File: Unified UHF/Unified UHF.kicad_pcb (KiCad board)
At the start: 2 copper layers, 82.5 x 82.5 mm, 82 parts, among them IC1 QPC1022SR, IC2 GRF5504, IC3 LHA-13LN+, IC4 QPC1022SR, J1 Conn_01x05, J2 Conn_01x02, J3 Conn_01x02, J4 Conn_01x01, J5 PCB.SMAFST.2H.A.HT, U1 AT86RF215-ZU, U2 NCS-62+, X1 TYETACSANF-26.000000

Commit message: small changes
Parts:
- H1, H2, H3, H4: footprint MountingHole:MountingHole_3.2mm_M3 -> MountingHole:MountingHole_3.5mm_Pad
- moved C4 0.58 mm to (37.8, 66.1)
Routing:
- net GND: track 198.8 -> 189.3 mm, vias 2973 -> 2977

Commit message: Routed coax
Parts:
- moved J5 5.60 mm to (88.0, 26.2)
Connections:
- C3 pad 1: GND -> GNDD
- C4 pad 1: GND -> GNDD
- C5 pad 1: GND -> GNDD
- C6 pad 1: GND -> GNDD
- U1 pad 20: GND -> GNDD
- U1 pad 23: GND -> GNDD
- U1 pad 24: GND -> GNDD
- U1 pad 32: GND -> GNDD
- U1 pad 38: GND -> GNDD
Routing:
- net Net-(IC4-ANT): track 4.63 -> 46.9 mm
- net GND: track 189.3 -> 162.8 mm, vias 2977 -> 3321
- net GNDD: track 0.00 -> 14.5 mm, vias 0 -> 8
- net Net-(U1-RFN09): track 8.53 -> 7.21 mm
- net Net-(U1-FEA09): track 36.3 -> 37.4 mm, vias 1 -> 0
- added copper zone on B.Cu, net GNDD
- added copper zone on F.Cu, net GNDD
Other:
- board text added: "PVDX UHF BOARD"
- board text removed: "PVDX UHF FRONTEND"

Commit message: adjustments
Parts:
- moved J5 67.6 mm to (88.2, 93.8)
- moved G*** 33.9 mm to (55.0, 87.2)
- moved C28 7.83 mm to (100.8, 68.4)
- moved TP13 7.41 mm to (101.8, 61.0)
- moved C25 7.36 mm to (101.6, 71.2), turned to 0 degrees
- moved C24 4.45 mm to (101.6, 73.2), turned to 0 degrees
- moved TP14 2.89 mm to (104.6, 53.4)
- moved L5 1.77 mm to (100.4, 75.2)
- moved C3 1.52 mm to (39.4, 53.8), turned to 0 degrees
- moved L4 1.50 mm to (97.6, 74.2)
- moved TP2 1.34 mm to (35.6, 55.2)
- moved C5 1.14 mm to (35.4, 60.6), turned to 90 degrees
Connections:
- H1 pad 1: (no net) -> GND
- H2 pad 1: (no net) -> GND
- H3 pad 1: (no net) -> GND
- H4 pad 1: (no net) -> GND
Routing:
- net Net-(IC4-RF1): track 27.2 -> 19.7 mm
- net Net-(IC4-ANT): track 46.9 -> 53.5 mm
- net Net-(C24-Pad1): track 7.76 -> 4.06 mm
- net +5V: track 143.1 -> 141.6 mm
- net +3V3: track 112.0 -> 113.2 mm
- net Net-(IC2-RF_OUT/VCC2_1): track 7.26 -> 6.18 mm
- net Net-(U1-CLKO): track 5.56 -> 6.41 mm
- net GND: track 162.8 -> 162.6 mm, vias 3321 -> 2852
- removed copper zone on B.Cu, net GNDD
- removed copper zone on F.Cu, net GNDD

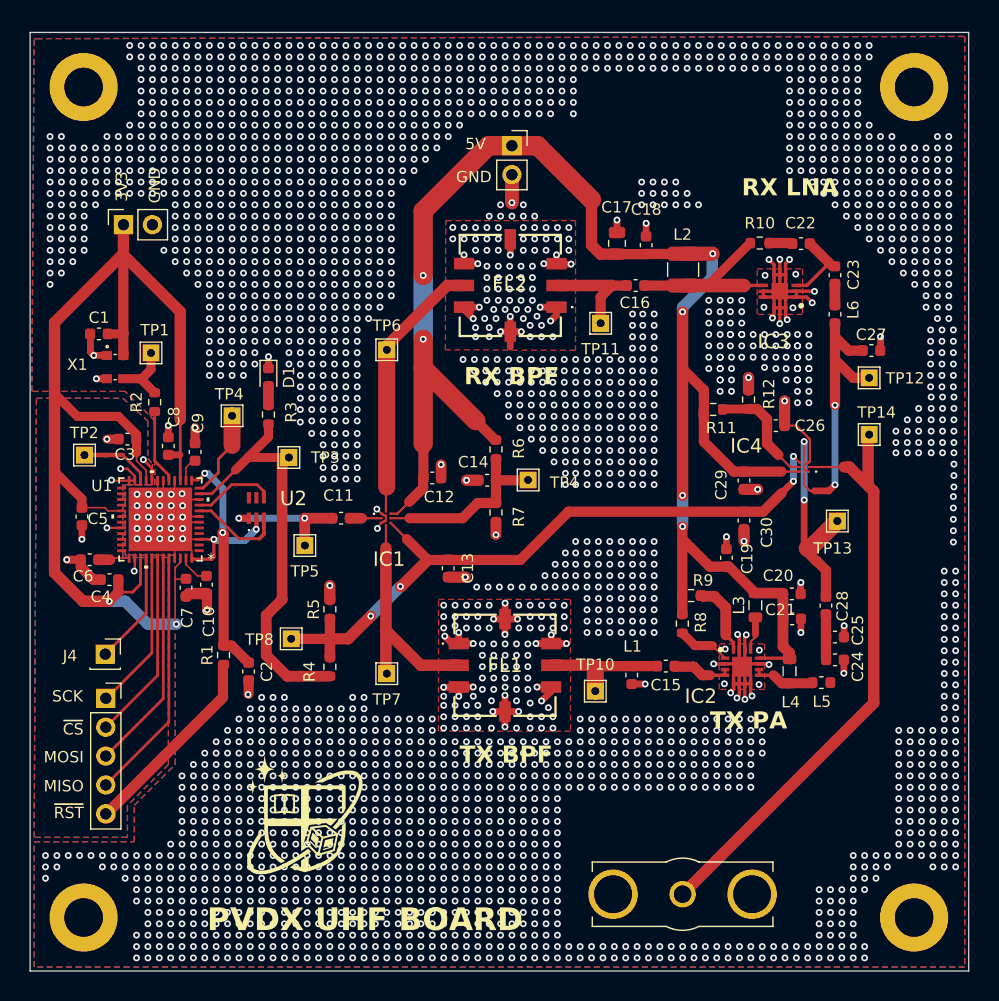
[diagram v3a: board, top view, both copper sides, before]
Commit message: added connector, changed connection to under paddle, other neurotic fixes
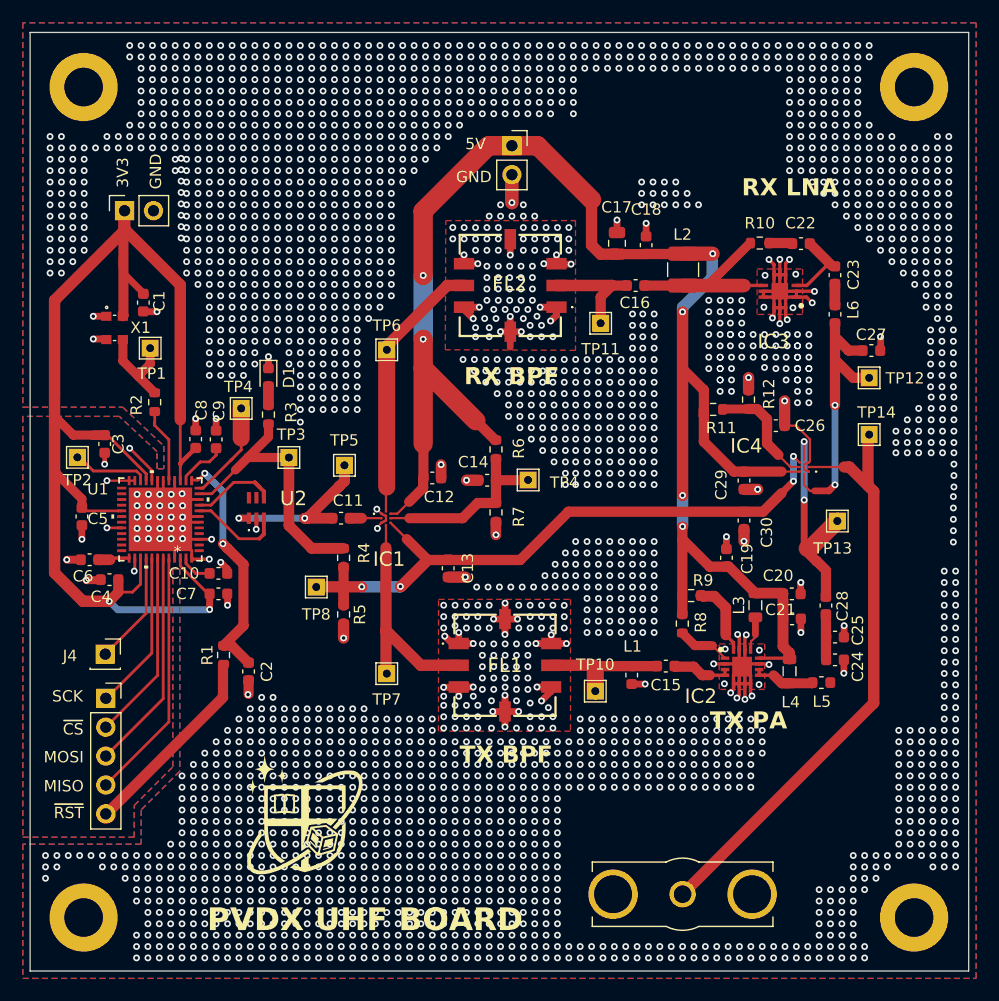
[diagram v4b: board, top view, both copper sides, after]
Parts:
- moved R4 9.66 mm to (58.4, 64.2), turned to -90 degrees
- moved TP5 7.86 mm to (58.5, 56.1)
- moved TP8 5.06 mm to (56.0, 66.8)
- moved C1 4.77 mm to (40.8, 41.8), turned to 90 degrees
- moved X1 3.44 mm to (43.3, 44.0)
- moved C7 2.90 mm to (47.4, 67.4), turned to 180 degrees
- moved C8 2.48 mm to (45.4, 53.8)
- moved C9 2.15 mm to (47.2, 53.8)
- moved C3 2.04 mm to (37.4, 54.2), turned to 90 degrees
- moved C10 1.45 mm to (47.4, 65.6), turned to 180 degrees
- moved R5 1.29 mm to (58.4, 69.2), turned to -90 degrees
- moved J3 1.23 mm to (39.2, 33.7)
- moved TP4 1.03 mm to (49.4, 51.1)
- moved TP2 0.65 mm to (35.0, 55.4)
- moved TP1 0.43 mm to (41.4, 45.8), turned to 180 degrees
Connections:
- C3 pad 1: GNDD -> GND
- C4 pad 1: GNDD -> GND
- C5 pad 1: GNDD -> GND
- C6 pad 1: GNDD -> GND
- U1 pad 20: GNDD -> GND
- U1 pad 23: GNDD -> GND
- U1 pad 24: GNDD -> GND
- U1 pad 32: GNDD -> GND
- U1 pad 38: GNDD -> GND
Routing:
- net GNDD: track 14.8 -> 0.00 mm, vias 8 -> 0
- net Net-(U1-FEA09): track 37.4 -> 24.5 mm
- net +3V3: track 113.2 -> 124.0 mm
- net GND: track 162.6 -> 167.3 mm, vias 2852 -> 2803
- net Net-(IC1-CTRL): track 60.9 -> 56.8 mm
- net Net-(C11-Pad1): track 11.3 -> 15.1 mm
- net Net-(X1-OUT): track 5.41 -> 8.39 mm
- net Net-(U1-AVDD0): track 2.00 -> 4.42 mm
- net Net-(U1-RSTN): track 20.2 -> 21.5 mm
- net Net-(U1-FEB09): track 7.72 -> 8.88 mm
- net Net-(U1-RFN09): track 7.21 -> 7.94 mm

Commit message: small change
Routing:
- net GND: vias 2803 -> 2793
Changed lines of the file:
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@@
 	)
 	(via
-		(at 44.122069 29.103893)
-		(size 0.6)
-		(drill 0.3)
-		(layers "F.Cu" "B.Cu")
-		(free yes)
-		(teardrops
-			(best_length_ratio 0.5)
-			(max_length 1)
-			(best_width_ratio 1)
-			(max_width 2)
-			(curved_edges no)
-			(filter_ratio 0.9)
-			(enabled yes)
-			(allow_two_segments yes)
-			(prefer_zone_connections yes)
-		)
-		(net "GND")
-	)
-	(via
 		(at 111.203477 90.385301)
 		(size 0.6)
@@
 	)
 	(via
-		(at 44.122069 31.103893)
-		(size 0.6)
-		(drill 0.3)
-		(layers "F.Cu" "B.Cu")
-		(free yes)
-		(teardrops
-			(best_length_ratio 0.5)
-			(max_length 1)
-			(best_width_ratio 1)
-			(max_width 2)
-			(curved_edges no)
-			(filter_ratio 0.9)
-			(enabled yes)
-			(allow_two_segments yes)
-			(prefer_zone_connections yes)
-		)
-		(net "GND")
-	)
-	(via
 		(at 40.253477 59.635301)
 		(size 0.6)
@@
 	)
 	(via
-		(at 44.122069 30.103893)
-		(size 0.6)
-		(drill 0.3)
-		(layers "F.Cu" "B.Cu")
-		(free yes)
-		(teardrops
-			(best_length_ratio 0.5)
-			(max_length 1)
-			(best_width_ratio 1)
-			(max_width 2)
-			(curved_edges no)
-			(filter_ratio 0.9)
-			(enabled yes)
-			(allow_two_segments yes)
-			(prefer_zone_connections yes)
-		)
-		(net "GND")
-	)
-	(via
 		(at 71.203477 83.385301)
 		(size 0.6)
@@
 	)
 	(via
-		(at 44.122069 32.103893)
-		(size 0.6)
-		(drill 0.3)
-		(layers "F.Cu" "B.Cu")
-		(free yes)
-		(teardrops
-			(best_length_ratio 0.5)
-			(max_length 1)
-			(best_width_ratio 1)
-			(max_width 2)
-			(curved_edges no)
-			(filter_ratio 0.9)
-			(enabled yes)
-			(allow_two_segments yes)
-			(prefer_zone_connections yes)
-		)
-		(net "GND")
-	)
-	(via
 		(at 72.003477 38.585301)
 		(size 0.6)
@@
 	)
 	(via
-		(at 43.603477 29.185301)
-		(size 0.6)
-		(drill 0.3)
-		(layers "F.Cu" "B.Cu")
-		(free yes)
-		(teardrops
-			(best_length_ratio 0.5)
-			(max_length 1)
-			(best_width_ratio 1)
-			(max_width 2)
-			(curved_edges no)
-			(filter_ratio 0.9)
-			(enabled yes)
-			(allow_two_segments yes)
-			(prefer_zone_connections yes)
-		)
-		(net "GND")
-	)
-	(via
 		(at 76.203477 85.385301)
 		(size 0.6)
@@
 	)
 	(via
-		(at 44.122069 36.103893)
-		(size 0.6)
-		(drill 0.3)
-		(layers "F.Cu" "B.Cu")
-		(free yes)
-		(teardrops
-			(best_length_ratio 0.5)
-			(max_length 1)
-			(best_width_ratio 1)
-			(max_width 2)
-			(curved_edges no)
-			(filter_ratio 0.9)
-			(enabled yes)
-			(allow_two_segments yes)
-			(prefer_zone_connections yes)
-		)
-		(net "GND")
-	)
-	(via
 		(at 59.603477 25.185301)
 		(size 0.6)
@@
 	)
 	(via
-		(at 44.122069 35.103893)
-		(size 0.6)
-		(drill 0.3)
-		(layers "F.Cu" "B.Cu")
-		(free yes)
-		(teardrops
-			(best_length_ratio 0.5)
-			(max_length 1)
-			(best_width_ratio 1)
-			(max_width 2)
-			(curved_edges no)
-			(filter_ratio 0.9)
-			(enabled yes)
-			(allow_two_segments yes)
-			(prefer_zone_connections yes)
-		)
-		(net "GND")
-	)
-	(via
 		(at 47.603477 42.185301)
 		(size 0.6)
@@
 	)
 	(via
-		(at 43.603477 30.185301)
-		(size 0.6)
-		(drill 0.3)
-		(layers "F.Cu" "B.Cu")
-		(free yes)
-		(teardrops
-			(best_length_ratio 0.5)
-			(max_length 1)
-			(best_width_ratio 1)
-			(max_width 2)
-			(curved_edges no)
-			(filter_ratio 0.9)
-			(enabled yes)
-			(allow_two_segments yes)
-			(prefer_zone_connections yes)
-		)
-		(net "GND")
-	)
-	(via
 		(at 69.203477 84.385301)
 		(size 0.6)
@@
 	)
 	(via
-		(at 44.122069 33.103893)
-		(size 0.6)
-		(drill 0.3)
-		(layers "F.Cu" "B.Cu")
-		(free yes)
-		(teardrops
-			(best_length_ratio 0.5)
-			(max_length 1)
-			(best_width_ratio 1)
-			(max_width 2)
-			(curved_edges no)
-			(filter_ratio 0.9)
-			(enabled yes)
-			(allow_two_segments yes)
-			(prefer_zone_connections yes)
-		)
-		(net "GND")
-	)
-	(via
 		(at 50.603477 36.185301)
 		(size 0.6)
@@
 		(size 0.6)
 		(drill 0.3)
-		(layers "F.Cu" "B.Cu")
-		(free yes)
-		(teardrops
-			(best_length_ratio 0.5)
-			(max_length 1)
-			(best_width_ratio 1)
-			(max_width 2)
-			(curved_edges no)
-			(filter_ratio 0.9)
-			(enabled yes)
-			(allow_two_segments yes)
-			(prefer_zone_connections yes)
-		)
-		(net "GND")
-	)
-	(via
-		(at 44.122069 34.103893)
-		(size 0.6)
-		(drill 0.3)

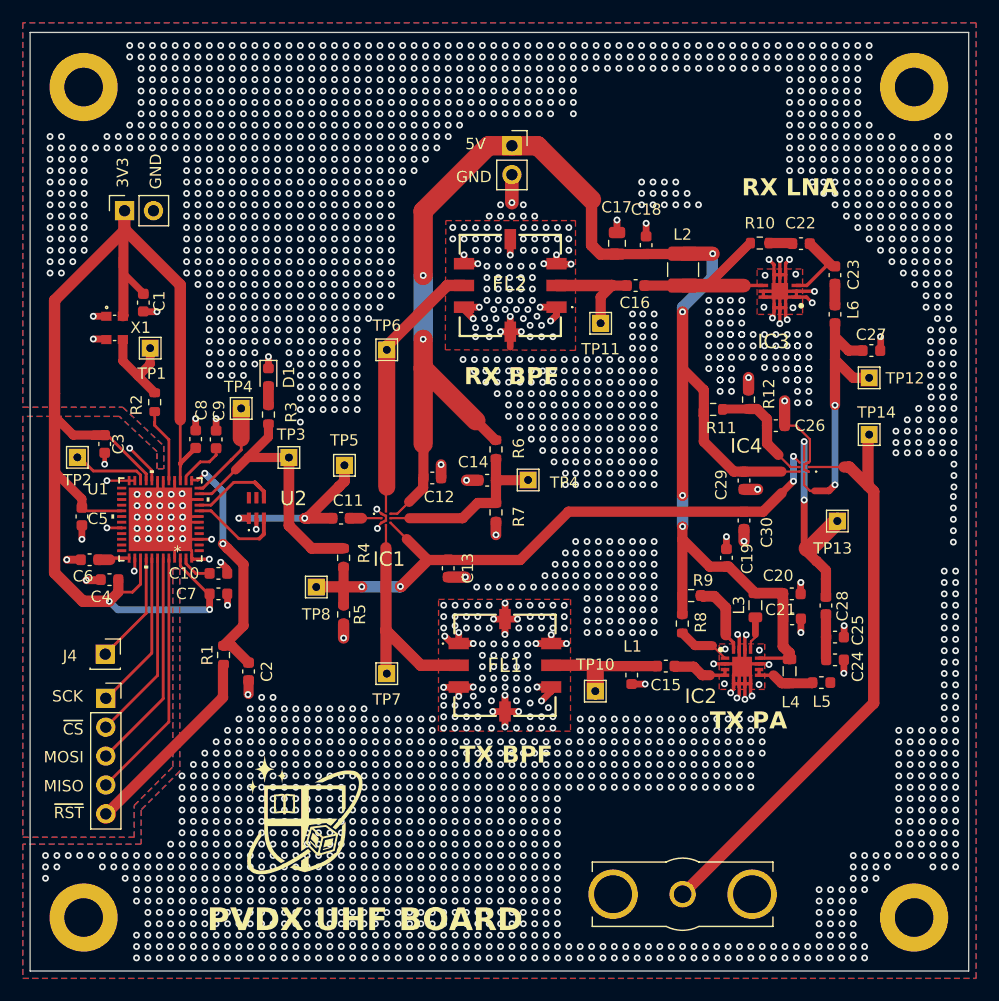
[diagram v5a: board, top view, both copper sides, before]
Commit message: design review, 3d models, silkscreen fix
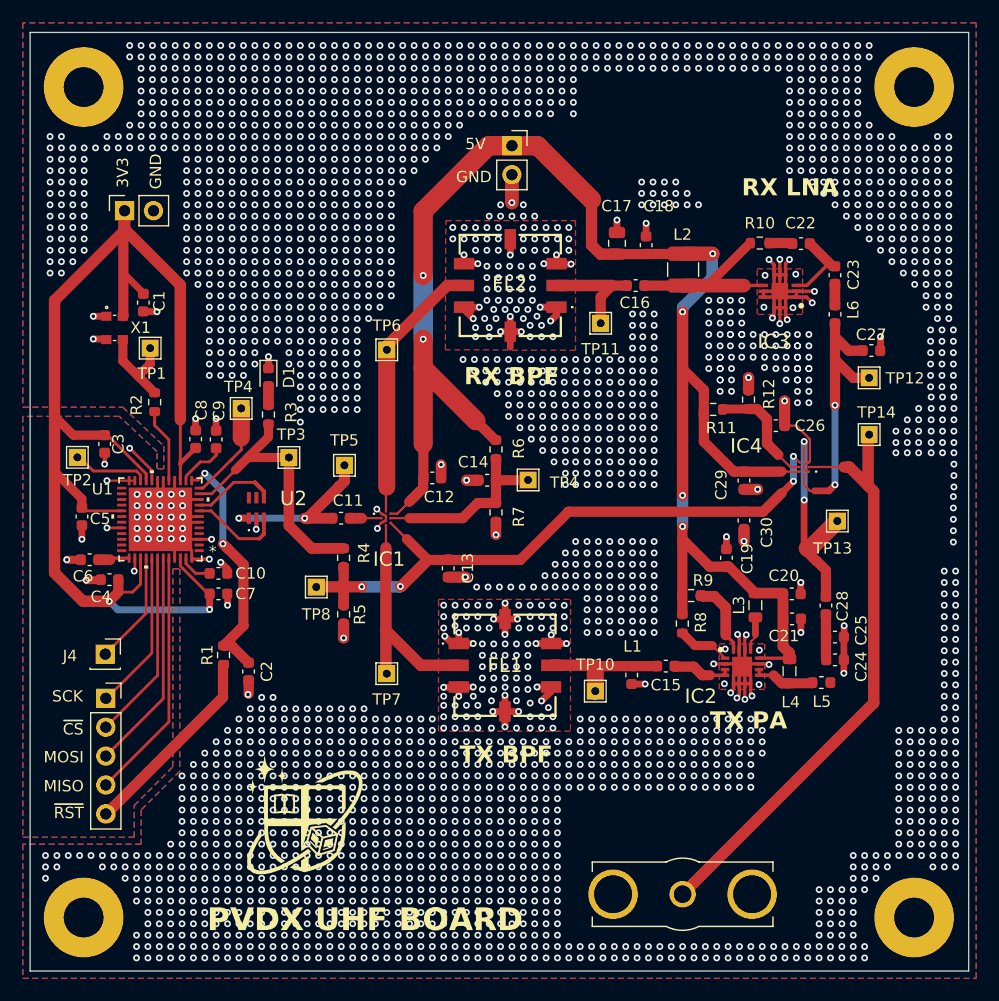
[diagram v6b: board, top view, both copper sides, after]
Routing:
- net GND: track 167.3 -> 169.3 mm
- net +3V3: track 124.0 -> 123.0 mm

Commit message: fixes fixes
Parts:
- C11: value 0.8p -> 10p
- J5: moved to B.Cu
- moved J5 2.41 mm to (88.2, 91.4), turned to 180 degrees
- moved TP3 2.28 mm to (55.2, 53.8)
- moved C11 1.84 mm to (56.4, 61.2), turned to 90 degrees
- moved TP5 0.93 mm to (59.4, 56.1)
- moved U2 0.66 mm to (51.4, 59.8), turned to -90 degrees
- moved IC1 0.26 mm to (62.1, 60.5)
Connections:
- C11 pad 1: Net-(C11-Pad1) -> GND
- TP5 pad 1: Net-(C11-Pad1) -> Net-(IC1-ANT)
- U2 pad 1: Net-(C11-Pad1) -> Net-(U1-RFN09)
- U2 pad 4: Net-(U1-RFN09) -> Net-(IC1-ANT)
- U2 pad 6: (no net) -> GND
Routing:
- net Net-(IC1-ANT): track 2.77 -> 18.0 mm
- net Net-(C11-Pad1): track 15.1 -> 0.00 mm, vias 2 -> 0
- net GND: track 169.3 -> 173.4 mm, vias 2793 -> 3550
- net Net-(U1-RFP09): track 8.24 -> 4.94 mm
- net Net-(U1-RFN09): track 7.94 -> 4.94 mm
- net Net-(IC4-ANT): track 53.5 -> 51.1 mm
- net Net-(C24-Pad1): track 4.06 -> 6.19 mm
- net Net-(U1-FEA09): track 24.5 -> 26.5 mm, vias 0 -> 2
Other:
- board text removed: "BSE"
